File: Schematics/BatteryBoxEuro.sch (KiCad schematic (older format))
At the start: 16 parts, among them K1 JD2912-1Z-12VDC_40A, P1 Conn_WallPlug, U2 F_Distributor, U3 NAC3MPA-1-WOT, U4 DPlusSimulator, U5 Pulser, U6 230V_KfzCharger, X1 X3, X2 12VKfz_Plug, X3 X3

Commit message: add filed
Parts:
- removed P1: Conn_WallPlug, symbol Connector:Conn_WallPlug
- removed U3, U?: NAC3MPA-1-WOT, NAC3MPA-1-WOT, symbol NAC3MPA-1-WOT:NAC3MPA-1-WOT
- removed U?: Terminal16, symbol MyParts:Terminal16
- removed X2: 12VKfz_Plug, symbol MyParts:12VKfz_Plug
- added BT1: 12V, symbol Device:Battery
- added J1, J4: (no value), symbol Connector:Conn_01x02_Female
- added J2, J3: (no value), symbol Connector:Conn_01x02_Male
- added P?: Conn_WallPlug_Earth, symbol Connector:Conn_WallPlug_Earth
- added U1: Terminal16, symbol MyParts:Terminal16
- added U3: PB12V-Charger, symbol MyParts:PB12V-Charger
- renumbered K1 to K?, U6 to U?, X1 to X?
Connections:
- wire segments 65 -> 90
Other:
- moved on the sheet: F2, K?, U2, U4, U5, X3, X?

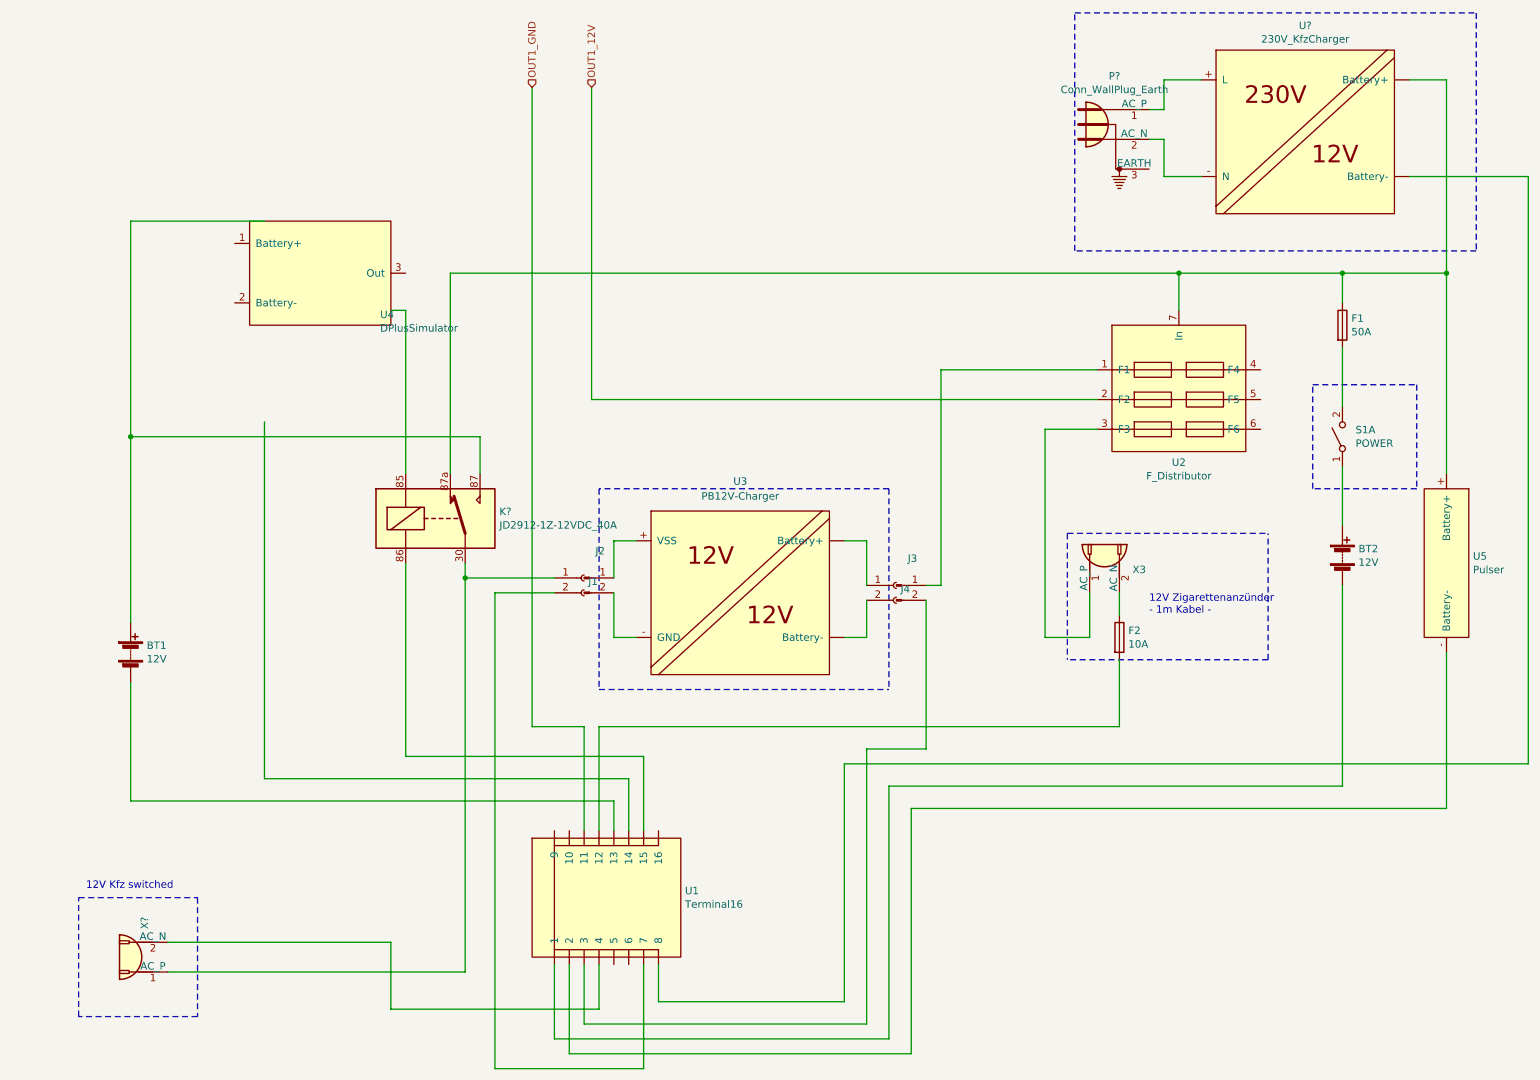
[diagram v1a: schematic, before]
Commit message: add 230V
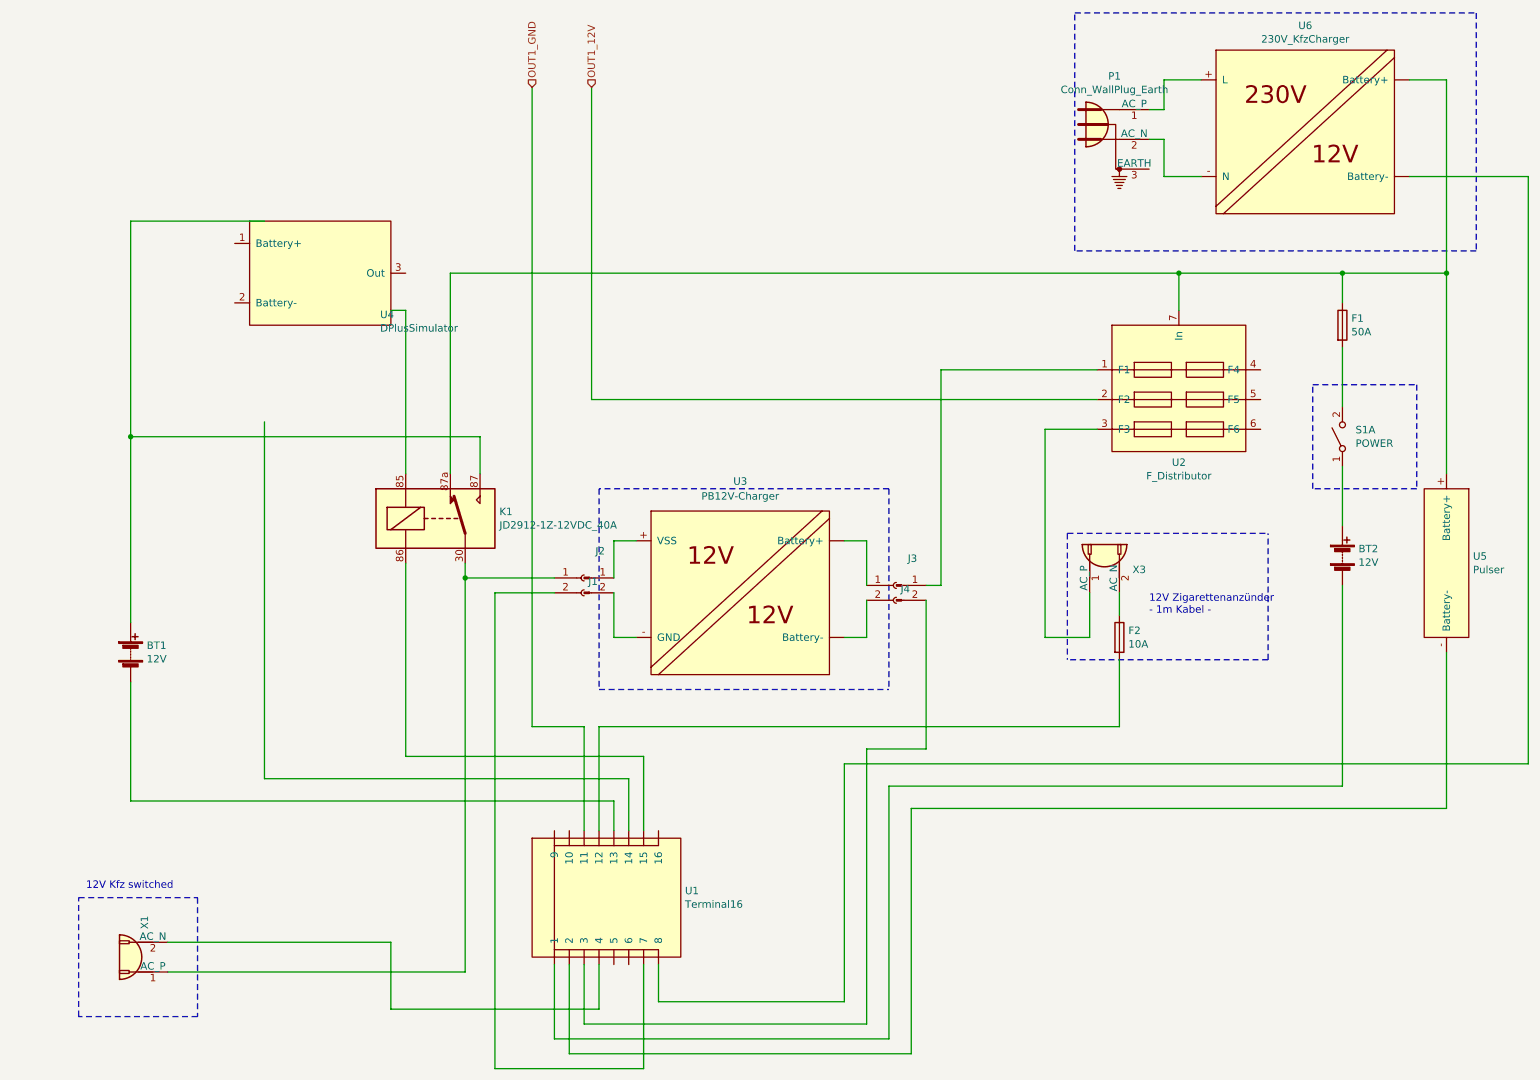
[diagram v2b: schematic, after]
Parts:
- gave numbers to parts that had none: 4
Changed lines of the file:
@@
 12V Zigarettenanzünder\n- 1m Kabel -
 $Comp
-L Connector:Conn_WallSocket X?
+L Connector:Conn_WallSocket X1
 U 1 1 5EC190DC
 P 1500 6950
-F 0 "X?" V 1456 6762 50  0000 R CNN
+F 0 "X1" V 1456 6762 50  0000 R CNN
 F 1 "X3" V 1411 6762 50  0001 R CNN
 F 2 "" H 1100 6950 50  0001 C CNN
@@
 	3900 4500 3900 7700
 $Comp
-L MyParts:230V_KfzCharger U?
+L MyParts:230V_KfzCharger U6
 U 1 1 5EC5CF8F
 P 9150 750
-F 0 "U?" H 9350 815 50  0000 C CNN
+F 0 "U6" H 9350 815 50  0000 C CNN
 F 1 "230V_KfzCharger" H 9350 724 50  0000 C CNN
 F 2 "" H 9150 750 50  0001 C CNN
@@
 	7800 2200 7800 600
 $Comp
-L Connector:Conn_WallPlug_Earth P?
+L Connector:Conn_WallPlug_Earth P1
 U 1 1 5ECE1CC2
 P 8000 1350
-F 0 "P?" H 8067 1675 50  0000 C CNN
+F 0 "P1" H 8067 1675 50  0000 C CNN
 F 1 "Conn_WallPlug_Earth" H 8067 1584 50  0000 C CNN
 F 2 "" H 8400 1350 50  0001 C CNN
@@
 	8400 1700 8650 1700
 $Comp
-L MyParts:JD2912-1Z-12VDC_40A K?
+L MyParts:JD2912-1Z-12VDC_40A K1
 U 1 1 5EF13C07
 P 3500 4000
-F 0 "K?" H 3930 4046 50  0000 L CNN
+F 0 "K1" H 3930 4046 50  0000 L CNN
 F 1 "JD2912-1Z-12VDC_40A" H 3930 3955 50  0000 L CNN
 F 2 "Relay_THT:Relay_StandexMeder_DIP_LowProfile" H 3950 3950 50  0001 L CNN

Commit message: add Neutrik socket
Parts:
- removed P1: Conn_WallPlug_Earth, symbol Connector:Conn_WallPlug_Earth
- added P?: Conn_WallPlug, symbol Connector:Conn_WallPlug
- added U?: NAC3MPA-1-WOT, NAC3MPA-1-WOT, symbol NAC3MPA-1-WOT:NAC3MPA-1-WOT
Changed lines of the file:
@@
 	4600 5150 6550 5150
 Wire Wire Line
-	4500 5400 4150 5400
+	4500 5400 4350 5400
 Wire Wire Line
 	8500 2350 9600 2350
@@
 Wire Notes Line
 	7800 2200 7800 600
-$Comp
-L Connector:Conn_WallPlug_Earth P1
-U 1 1 5ECE1CC2
-P 8000 1350
-F 0 "P1" H 8067 1675 50  0000 C CNN
-F 1 "Conn_WallPlug_Earth" H 8067 1584 50  0000 C CNN
-F 2 "" H 8400 1350 50  0001 C CNN
-F 3 "~" H 8400 1350 50  0001 C CNN
-	1    8000 1350
-	1    0    0    -1
-$EndComp
 Wire Wire Line
 	8300 1250 8400 1250
@@
 	3600 2350 3600 3700
 Connection ~ 8500 2350
-Text HLabel 4550 1100 1    50   Input ~ 0
+Text HLabel 4550 1350 1    50   Input ~ 0
 OUT1_12V
-Text HLabel 4150 1100 1    50   Input ~ 0
+Text HLabel 4350 1350 1    50   Input ~ 0
 OUT1_GND
 Wire Wire Line
-	4550 3200 4550 1100
+	4550 3200 7950 3200
+$Comp
+L NAC3MPA-1-WOT:NAC3MPA-1-WOT U?
+U 1 1 5EF1E21B
+P 4150 1450
+F 0 "U?" V 3911 2080 50  0000 L CNN
+F 1 "NAC3MPA-1-WOT" V 4002 2080 50  0000 L CNN
+F 2 "NAC3MPA-1-WOT" H 4150 1450 50  0001 L BNN
+F 3 "" H 4150 1450 50  0001 C CNN
+	1    4150 1450
+	0    1    1    0
+$EndComp
 Wire Wire Line
-	4550 3200 7950 3200
+	4550 3200 4550 1650
 Wire Wire Line
-	4150 5400 4150 1100
+	4350 1650 4350 5400
+$Comp
+L Connector:Conn_WallPlug P?
+U 1 1 5EF29B60
+P 8100 1350
+F 0 "P?" H 8117 1675 50  0000 C CNN
+F 1 "Conn_WallPlug" H 8117 1584 50  0000 C CNN
+F 2 "" H 8500 1350 50  0001 C CNN
+F 3 "~" H 8500 1350 50  0001 C CNN
+	1    8100 1350
+	1    0    0    -1
+$EndComp
 $EndSCHEMATC

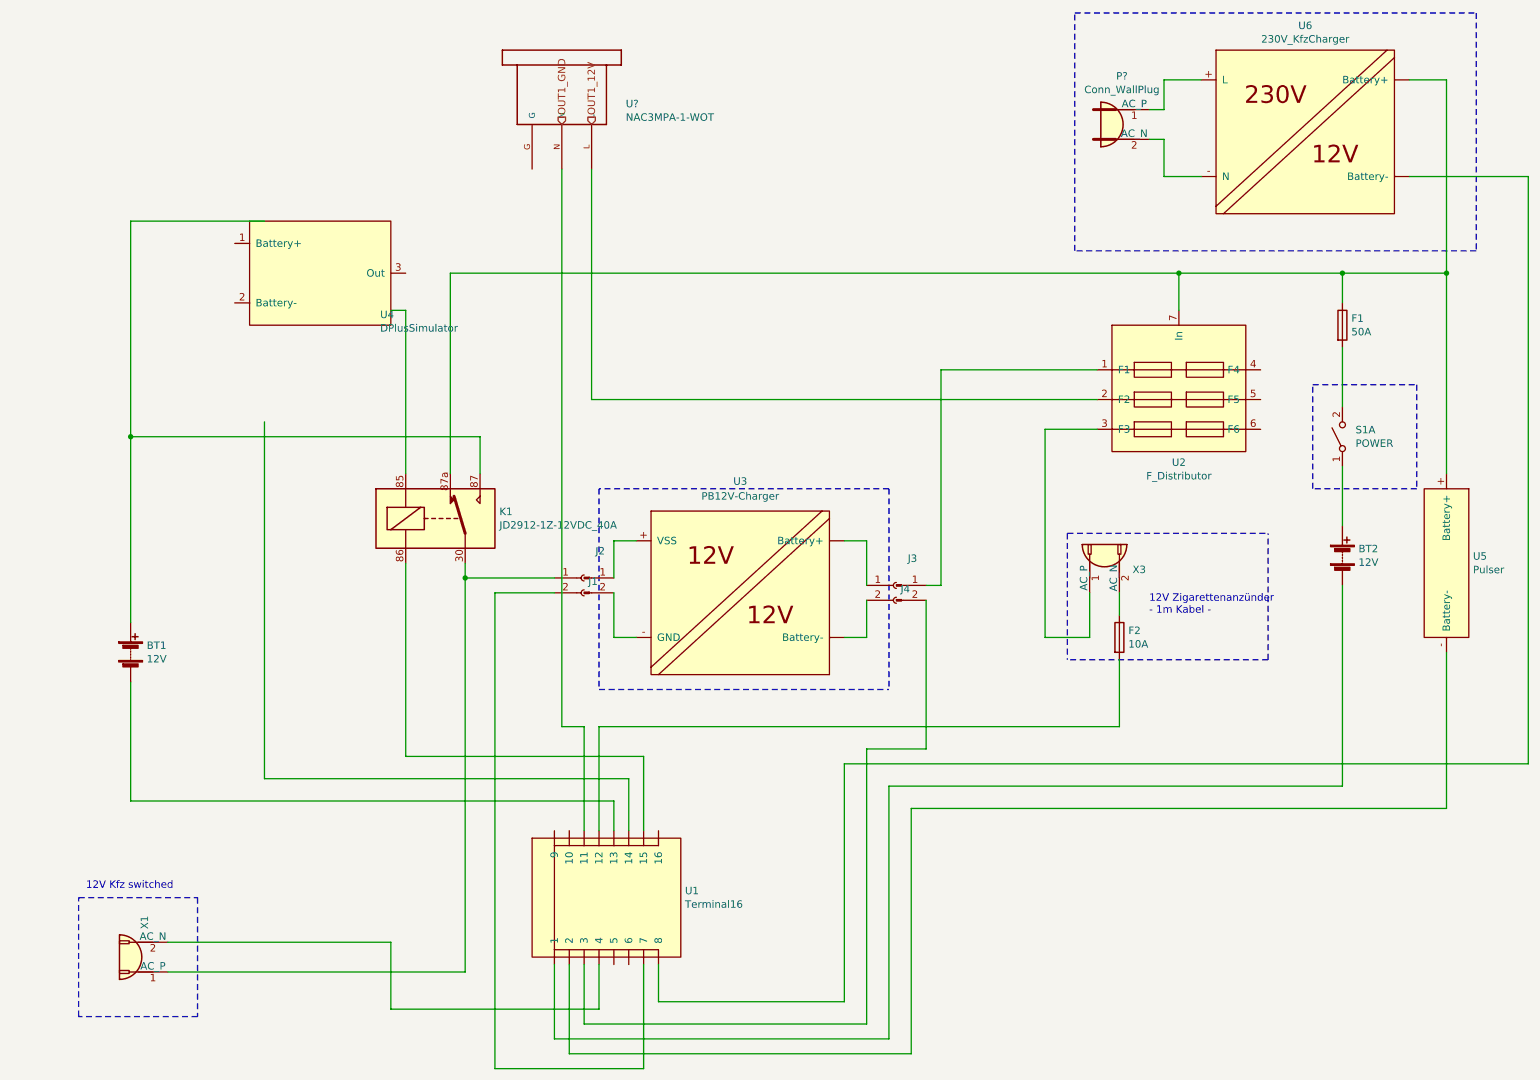
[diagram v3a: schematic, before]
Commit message: rearrange symbols
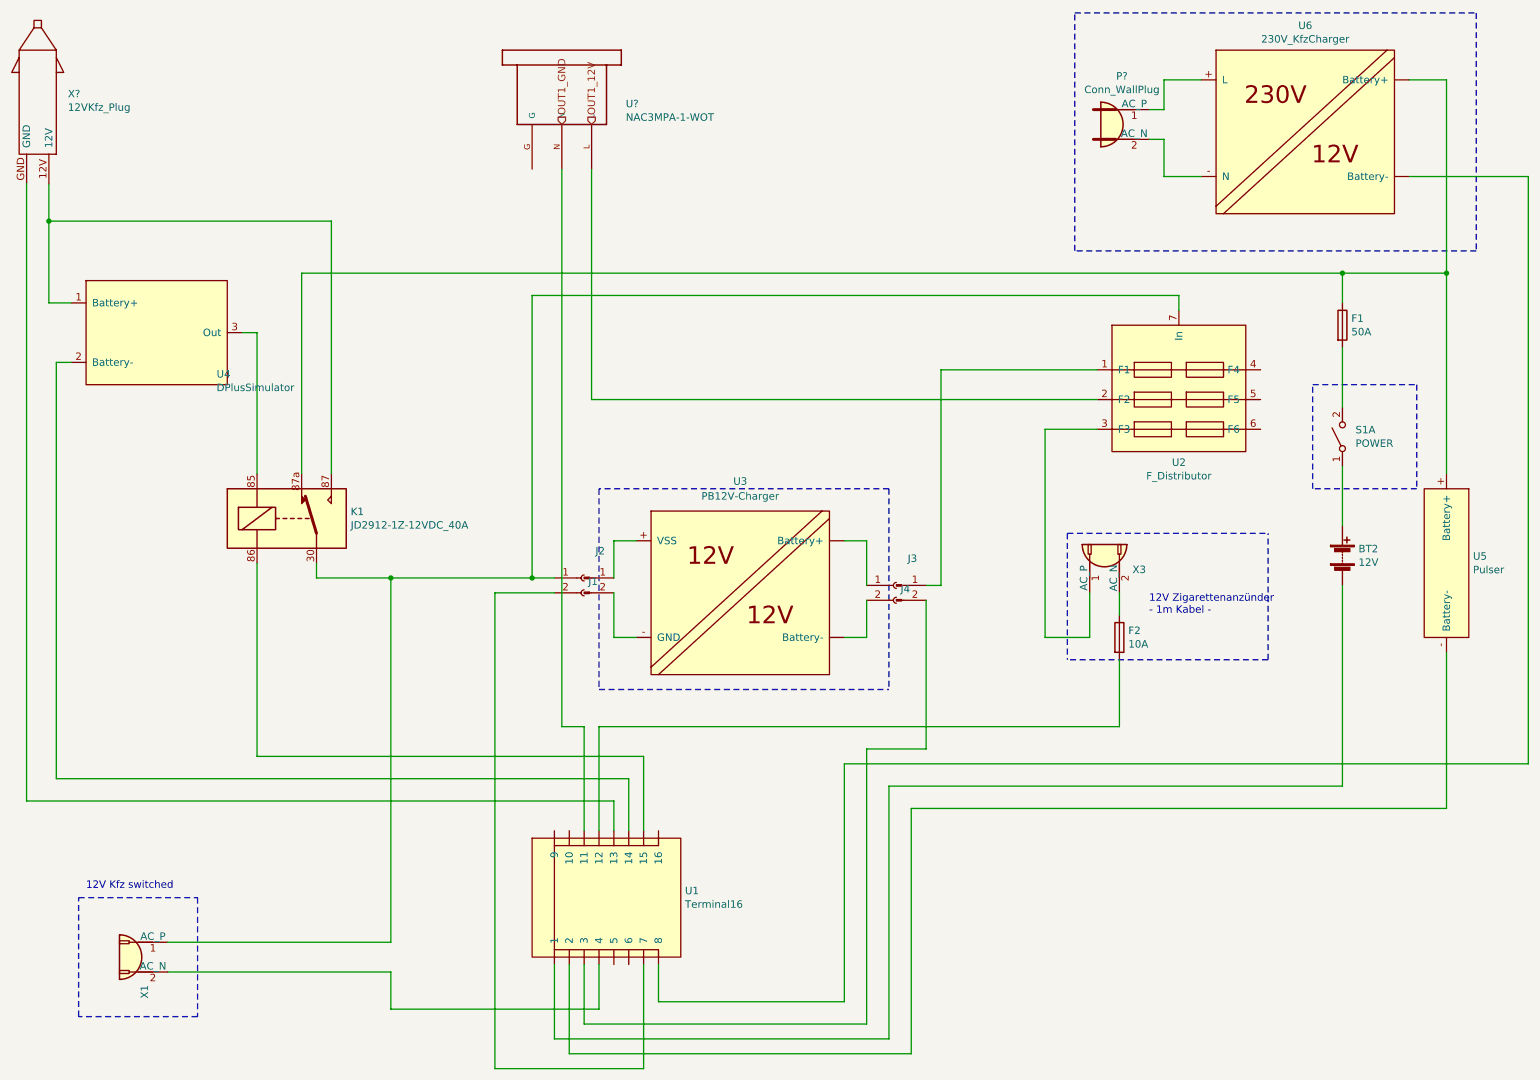
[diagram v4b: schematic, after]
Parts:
- removed BT1: 12V, symbol Device:Battery
- added X?: 12VKfz_Plug, symbol MyParts:12VKfz_Plug
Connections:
- wire segments 90 -> 94
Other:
- moved on the sheet: K1, U4
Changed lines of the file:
@@
 encoding utf-8
 Sheet 3 3
-Title ""
+Title "BatteryBox 400x300 Euro"
 Date ""
 Rev ""
@@
 $EndComp
 $Comp
-L Device:Battery BT1
-U 1 1 5E8737E8
-P 1450 4900
-F 0 "BT1" H 1558 4946 50  0000 L CNN
-F 1 "12V" H 1558 4855 50  0000 L CNN
-F 2 "" V 1450 4960 50  0001 C CNN
-F 3 "~" V 1450 4960 50  0001 C CNN
-	1    1450 4900
-	1    0    0    -1
-$EndComp
-$Comp
 L MyParts:DPlusSimulator U4
 U 1 1 5E87470E
-P 2250 2700
-F 0 "U4" H 3128 2771 50  0000 L CNN
-F 1 "DPlusSimulator" H 3128 2680 50  0000 L CNN
-F 2 "" H 2000 3200 50  0001 C CNN
-F 3 "" H 2000 3200 50  0001 C CNN
-	1    2250 2700
+P 1150 3100
+F 0 "U4" H 2028 3171 50  0000 L CNN
+F 1 "DPlusSimulator" H 2028 3080 50  0000 L CNN
+F 2 "" H 900 3600 50  0001 C CNN
+F 3 "" H 900 3600 50  0001 C CNN
+	1    1150 3100
 	1    0    0    -1
 $EndComp
@@
 	0    1    1    0
 $EndComp
-Wire Wire Line
-	1450 2000 1450 3450
 $Comp
 L MyParts:F_Distributor U2
@@
 Wire Wire Line
 	9600 2850 9600 3250
-Wire Wire Line
-	3200 2600 3300 2600
-Wire Wire Line
-	1450 2000 2350 2000
-Wire Wire Line
-	1450 3450 3800 3450
-Connection ~ 1450 3450
-Wire Wire Line
-	1450 3450 1450 4700
 $Comp
 L MyParts:PB12V-Charger U3
@@
 Wire Wire Line
 	4300 7000 4300 7500
-Wire Wire Line
-	1450 5100 1450 5900
-Wire Wire Line
-	2350 3350 2350 5750
 $Comp
 L Switch:SW_DPST_x2 S1
@@
 	4800 6100 4800 5750
 Wire Wire Line
-	4800 5750 2350 5750
+	4800 5750 950  5750
 Wire Wire Line
 	4900 6100 4900 5600
 Wire Wire Line
-	4900 5600 3300 5600
-Wire Wire Line
 	4700 6100 4700 5900
 Wire Wire Line
-	4700 5900 1450 5900
+	4700 5900 750  5900
 Wire Wire Line
 	4400 7000 4400 7600
@@
 Text Notes 8300 4650 0    50   ~ 0
 12V Zigarettenanzünder\n- 1m Kabel -
-$Comp
-L Connector:Conn_WallSocket X1
-U 1 1 5EC190DC
-P 1500 6950
-F 0 "X1" V 1456 6762 50  0000 R CNN
-F 1 "X3" V 1411 6762 50  0001 R CNN
-F 2 "" H 1100 6950 50  0001 C CNN
-F 3 "~" H 1100 6950 50  0001 C CNN
-	1    1500 6950
-	-1   0    0    1
-$EndComp
-Wire Wire Line
-	3700 4400 4300 4400
-Wire Wire Line
-	3700 7050 1700 7050
-Wire Wire Line
-	1700 6850 3200 6850
-Wire Wire Line
-	3200 6850 3200 7300
+Wire Wire Line
+	3200 4400 4150 4400
 Wire Wire Line
 	3200 7300 4600 7300
@@
 Wire Notes Line
 	6550 3800 6550 5150
-Wire Wire Line
-	3700 4400 3700 7050
 Wire Wire Line
 	3900 7700 4900 7700
@@
 	9600 4050 9600 3650
 Wire Wire Line
-	8500 2350 8500 2600
-Wire Wire Line
 	9600 2350 10300 2350
 Wire Wire Line
@@
 Wire Wire Line
 	4500 5400 4350 5400
-Wire Wire Line
-	8500 2350 9600 2350
-Connection ~ 9600 2350
 Wire Wire Line
 	10050 1050 10300 1050
@@
 L MyParts:JD2912-1Z-12VDC_40A K1
 U 1 1 5EF13C07
-P 3500 4000
-F 0 "K1" H 3930 4046 50  0000 L CNN
-F 1 "JD2912-1Z-12VDC_40A" H 3930 3955 50  0000 L CNN
-F 2 "Relay_THT:Relay_StandexMeder_DIP_LowProfile" H 3950 3950 50  0001 L CNN
-F 3 "https://standexelectronics.com/wp-content/uploads/datasheet_reed_relay_DIP.pdf" H 3500 4000 50  0001 C CNN
-	1    3500 4000
-	1    0    0    -1
-$EndComp
-Wire Wire Line
-	3700 4300 3700 4400
-Connection ~ 3700 4400
-Wire Wire Line
-	3300 4300 3300 5600
-Wire Wire Line
-	3300 2600 3300 3700
-Wire Wire Line
-	3800 3450 3800 3700
-Wire Wire Line
-	8500 2350 3600 2350
-Wire Wire Line
-	3600 2350 3600 3700
-Connection ~ 8500 2350
+P 2500 4000
+F 0 "K1" H 2930 4046 50  0000 L CNN
+F 1 "JD2912-1Z-12VDC_40A" H 2930 3955 50  0000 L CNN
+F 2 "Relay_THT:Relay_StandexMeder_DIP_LowProfile" H 2950 3950 50  0001 L CNN
+F 3 "https://standexelectronics.com/wp-content/uploads/datasheet_reed_relay_DIP.pdf" H 2500 4000 50  0001 C CNN
+	1    2500 4000
+	1    0    0    -1
+$EndComp
+Connection ~ 3200 4400
 Text HLabel 4550 1350 1    50   Input ~ 0
 OUT1_12V
@@
 	1    0    0    -1
 $EndComp
+Wire Wire Line
+	4150 4400 4150 2500
+Wire Wire Line
+	4150 2500 8500 2500
+Wire Wire Line
+	8500 2500 8500 2600
+Connection ~ 4150 4400
+Wire Wire Line
+	4150 4400 4300 4400
+Connection ~ 9600 2350
+Wire Wire Line
+	2600 3700 2600 2350
+Wire Wire Line
+	2700 4300 2700 4400
+Wire Wire Line
+	2700 4400 3200 4400
+Wire Wire Line
+	2300 5600 2300 4300
+Wire Wire Line
+	2300 5600 4900 5600
+Wire Wire Line
+	2200 2750 2300 2750
+Wire Wire Line
+	2600 2350 9600 2350
+Wire Wire Line
+	2800 2000 2800 3700
+$Comp
+L MyParts:12VKfz_Plug X?
+U 1 1 5EF8167C
+P 1050 1300
+F 0 "X?" V 1206 1278 50  0000 L CNN
+F 1 "12VKfz_Plug" V 1115 1278 50  0000 L CNN
+F 2 "" H 1050 1300 50  0001 C CNN
+F 3 "" H 1050 1300 50  0001 C CNN
+	1    1050 1300
+	0    1    -1   0
+$EndComp
+Wire Wire Line
+	750  1750 750  5900
+Wire Wire Line
+	900  2000 900  1750
+Wire Wire Line
+	900  2000 2800 2000
+Wire Wire Line
+	1050 2550 900  2550
+Connection ~ 900  2000
+Wire Wire Line
+	950  2950 1050 2950
+Wire Wire Line
+	900  2550 900  2000
+Wire Wire Line
+	950  2950 950  5750
+Wire Wire Line
+	2300 2750 2300 3700
+Wire Wire Line
+	3200 4400 3200 6850
+$Comp
+L Connector:Conn_WallSocket X1
+U 1 1 5EC190DC
+P 1500 6950
+F 0 "X1" V 1456 6762 50  0000 R CNN
+F 1 "X3" V 1411 6762 50  0001 R CNN
+F 2 "" H 1100 6950 50  0001 C CNN
+F 3 "~" H 1100 6950 50  0001 C CNN
+	1    1500 6950
+	-1   0    0    -1
+$EndComp
+Wire Wire Line
+	1700 6850 3200 6850
+Wire Wire Line
+	3200 7050 3200 7300
+Wire Wire Line
+	1700 7050 3200 7050
 $EndSCHEMATC
